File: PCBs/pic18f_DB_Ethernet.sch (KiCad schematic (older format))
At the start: 21 parts

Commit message: TODO: Programming header. TODO: incorporate cabling design for connector modules.
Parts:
- added C? (x2): CAP, symbol pspice:CAP
- added J? (x2): Conn02x05OddEven, symbol Connector_Generic:Conn_02x05_Odd_Even
- added R? (x3): R_US, symbol Device:R_US
- added SW?: SW_DPDT_x2, symbol Switch:SW_DPDT_x2
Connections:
- net 3v3: now also C?.1, C?.1, SW?.5 (B)
- net GNDREF: now also C?.2, C?.2, R?.2, R?.2, R?.2
- net at SW?.1 (A): now also R?.1
- new net: R?.1, SW?.6 (C)
- new net: R?.1, SW?.4 (A)
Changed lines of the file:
@@
 Wire Wire Line
 	2000 3300 2150 3300
+$Comp
+L Device:R_US R?
+U 1 1 5E534EAE
+P 2750 3450
+F 0 "R?" H 2818 3496 50  0000 L CNN
+F 1 "R_US" H 2818 3405 50  0000 L CNN
+F 2 "" V 2790 3440 50  0001 C CNN
+F 3 "~" H 2750 3450 50  0001 C CNN
+	1    2750 3450
+	1    0    0    -1
+$EndComp
+Text GLabel 2450 3600 0    50   Input ~ 0
+GND
+Wire Wire Line
+	2450 3600 2750 3600
+Wire Wire Line
+	2750 3300 2750 3100
+Wire Wire Line
+	2750 3100 2000 3100
+Text GLabel 1300 4050 0    50   Input ~ 0
+3v3
+Wire Wire Line
+	1300 4050 1600 4050
+$Comp
+L Device:R_US R?
+U 1 1 5E5368E4
+P 2150 4300
+F 0 "R?" H 2218 4346 50  0000 L CNN
+F 1 "R_US" H 2218 4255 50  0000 L CNN
+F 2 "" V 2190 4290 50  0001 C CNN
+F 3 "~" H 2150 4300 50  0001 C CNN
+	1    2150 4300
+	1    0    0    -1
+$EndComp
+Text GLabel 1850 4450 0    50   Input ~ 0
+GND
+Wire Wire Line
+	1850 4450 2150 4450
+Wire Wire Line
+	2000 4150 2150 4150
+$Comp
+L Device:R_US R?
+U 1 1 5E5368EE
+P 2750 4300
+F 0 "R?" H 2818 4346 50  0000 L CNN
+F 1 "R_US" H 2818 4255 50  0000 L CNN
+F 2 "" V 2790 4290 50  0001 C CNN
+F 3 "~" H 2750 4300 50  0001 C CNN
+	1    2750 4300
+	1    0    0    -1
+$EndComp
+Text GLabel 2450 4450 0    50   Input ~ 0
+GND
+Wire Wire Line
+	2450 4450 2750 4450
+Wire Wire Line
+	2750 4150 2750 3950
+Wire Wire Line
+	2750 3950 2000 3950
+$Comp
+L Switch:SW_DPDT_x2 SW?
+U 2 1 5E537BD7
+P 1800 4050
+F 0 "SW?" H 1800 4335 50  0000 C CNN
+F 1 "SW_DPDT_x2" H 1800 4244 50  0000 C CNN
+F 2 "" H 1800 4050 50  0001 C CNN
+F 3 "" H 1800 4050 50  0001 C CNN
+	2    1800 4050
+	1    0    0    -1
+$EndComp
+$Comp
+L Connector_Generic:Conn_02x05_Odd_Even J?
+U 1 1 5E53B6D7
+P 7350 2350
+F 0 "J?" V 7354 2630 50  0000 L CNN
+F 1 "Conn02x05OddEven" V 7445 2630 50  0000 L CNN
+F 2 "" H 7350 2350 50  0001 C CNN
+F 3 "~" H 7350 2350 50  0001 C CNN
+	1    7350 2350
+	0    1    1    0
+$EndComp
+$Comp
+L Connector_Generic:Conn_02x05_Odd_Even J?
+U 1 1 5E53C70C
+P 7350 3550
+F 0 "J?" V 7354 3830 50  0000 L CNN
+F 1 "Conn02x05OddEven" V 7445 3830 50  0000 L CNN
+F 2 "" H 7350 3550 50  0001 C CNN
+F 3 "~" H 7350 3550 50  0001 C CNN
+	1    7350 3550
+	0    1    1    0
+$EndComp
+$Comp
+L pspice:CAP C?
+U 1 1 5E53E1CC
+P 1800 4950
+F 0 "C?" H 1978 4996 50  0000 L CNN
+F 1 "CAP" H 1978 4905 50  0000 L CNN
+F 2 "" H 1800 4950 50  0001 C CNN
+F 3 "~" H 1800 4950 50  0001 C CNN
+	1    1800 4950
+	1    0    0    -1
+$EndComp
+$Comp
+L pspice:CAP C?
+U 1 1 5E53E5BB
+P 2350 4950
+F 0 "C?" H 2528 4996 50  0000 L CNN
+F 1 "CAP" H 2528 4905 50  0000 L CNN
+F 2 "" H 2350 4950 50  0001 C CNN
+F 3 "~" H 2350 4950 50  0001 C CNN
+	1    2350 4950
+	1    0    0    -1
+$EndComp
+Text GLabel 1300 4700 0    50   Input ~ 0
+3v3
+Text GLabel 1300 5200 0    50   Input ~ 0
+GND
+Wire Wire Line
+	1300 5200 1800 5200
+Connection ~ 1800 5200
+Wire Wire Line
+	1800 5200 2350 5200
+Wire Wire Line
+	1300 4700 1800 4700
+Connection ~ 1800 4700
+Wire Wire Line
+	1800 4700 2350 4700
 $EndSCHEMATC

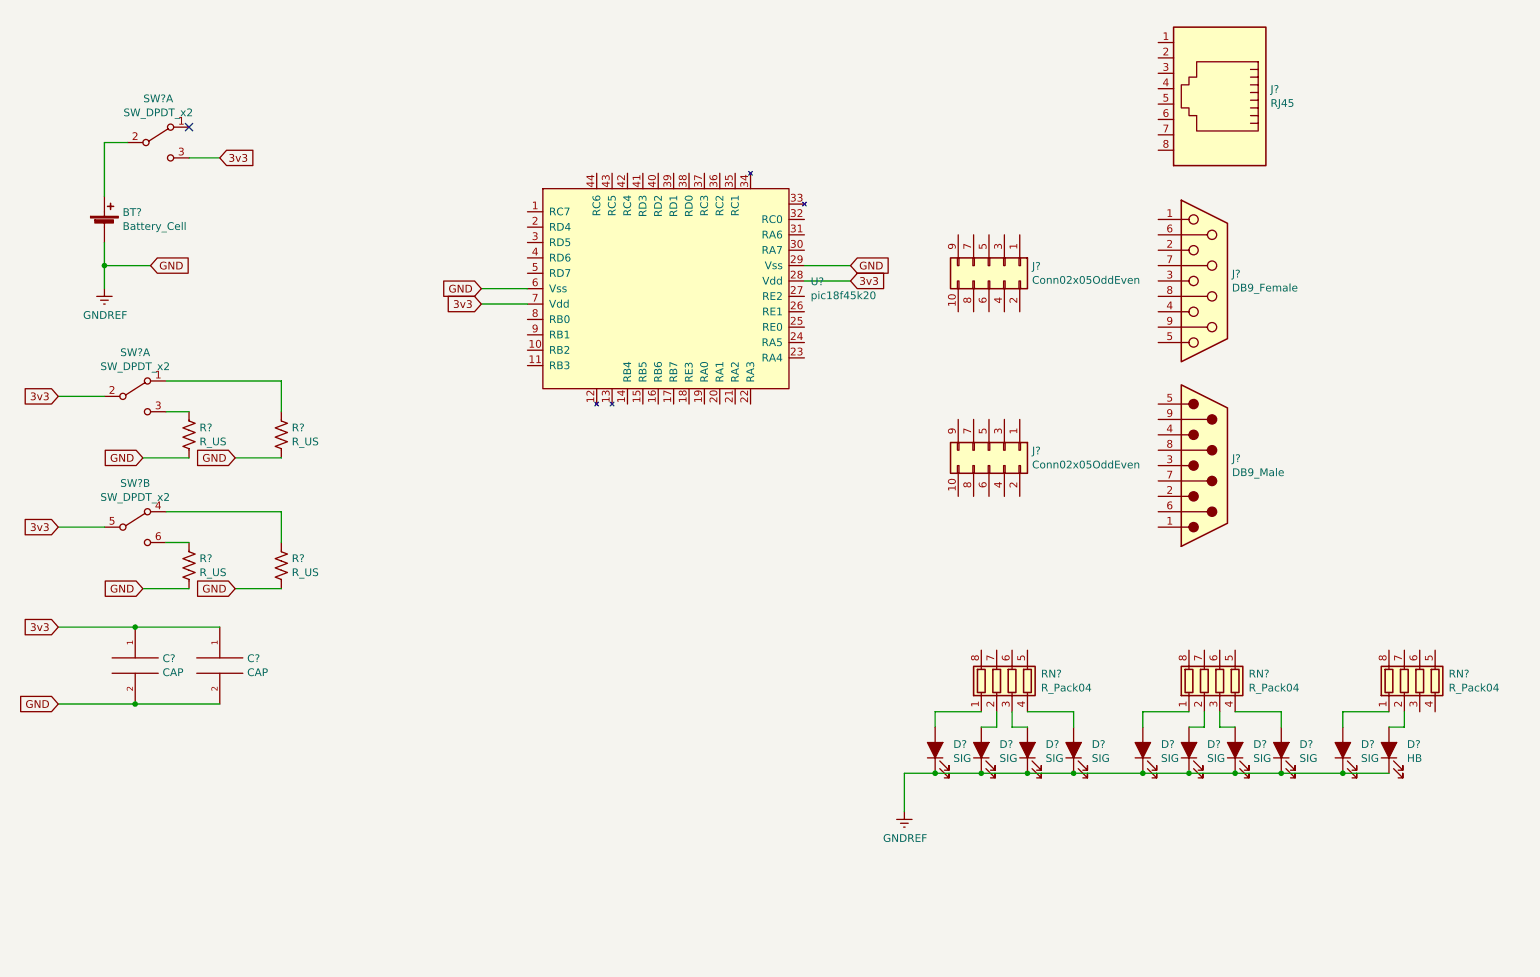
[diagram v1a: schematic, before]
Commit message: some basic connections laid down. TODO: double check I2C pins. Programming pins. And inputs.
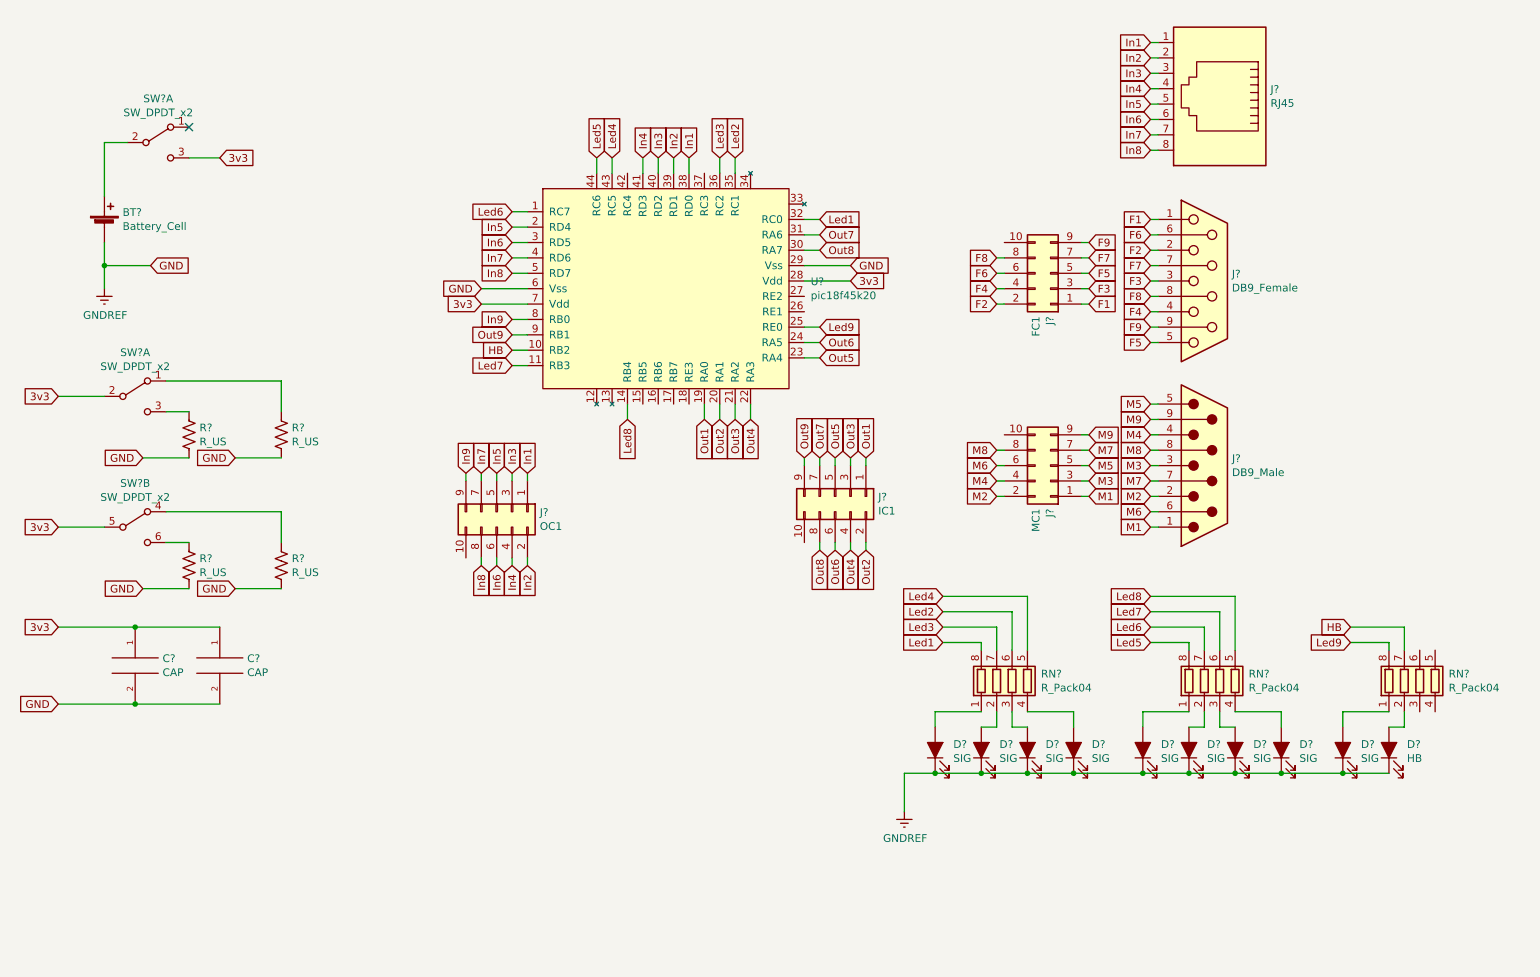
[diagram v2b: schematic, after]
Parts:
- added J?: OC1, symbol Connector_Generic:Conn_02x05_Odd_Even
- added J?: IC1, symbol Connector_Generic:Conn_02x05_Odd_Even
- J?: value Conn02x05OddEven -> FC1
- J?: value Conn02x05OddEven -> MC1
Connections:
- net In1: now reaches J?.1
- net In1: now also U?.38 (RD0), J?.1 (Pin_1)
- net In2: now reaches J?.2
- net In2: now also U?.39 (RD1), J?.2 (Pin_2)
- net In3: now reaches J?.3
- net In3: now also U?.40 (RD2), J?.3 (Pin_3)
- net In4: now reaches J?.4
- net In4: now also U?.41 (RD3), J?.4 (Pin_4)
- net In5: now reaches J?.5
- net In5: now also U?.2 (RD4), J?.5 (Pin_5)
- net In6: now reaches J?.6
- net In6: now also U?.3 (RD5), J?.6 (Pin_6)
- net In7: now reaches J?.7
- net In7: now also U?.4 (RD6), J?.7 (Pin_7)
- net In8: now reaches J?.8
- net In8: now also U?.5 (RD7), J?.8 (Pin_8)
- net F1: now reaches J?.1
- net F1: now also J?.1 (Pin_1)
- net F2: now reaches J?.2
- net F2: now also J?.2 (Pin_2)
- net F3: now reaches J?.3
- net F3: now also J?.3 (Pin_3)
- net F4: now reaches J?.4
- net F4: now also J?.4 (Pin_4)
- net F5: now reaches J?.5
- net F5: now also J?.5 (Pin_5)
- net F6: now reaches J?.6
- net F6: now also J?.6 (Pin_6)
- net F7: now reaches J?.7
- net F7: now also J?.7 (Pin_7)
- net F8: now reaches J?.8
- net F8: now also J?.8 (Pin_8)
- net F9: now reaches J?.9
- net F9: now also J?.9 (Pin_9)
- net M1: now reaches J?.1
- net M1: now also J?.1 (Pin_1)
- net M2: now reaches J?.2
- net M2: now also J?.2 (Pin_2)
- net M3: now reaches J?.3
- net M3: now also J?.3 (Pin_3)
- net M4: now reaches J?.4
- net M4: now also J?.4 (Pin_4)
- net M5: now reaches J?.5
- net M5: now also J?.5 (Pin_5)
- net M6: now reaches J?.6
- net M6: now also J?.6 (Pin_6)
- net M7: now reaches J?.7
- net M7: now also J?.7 (Pin_7)
- net M8: now reaches J?.8
- net M8: now also J?.8 (Pin_8)
- net M9: now reaches J?.9
- net M9: now also J?.9 (Pin_9)
- net Led4: now reaches RN?.5 (R4.2)
- net Led4: now also U?.43 (RC5)
- net Led2: now reaches RN?.6 (R3.2)
- net Led2: now also U?.35 (RC1)
- net Led3: now reaches RN?.7 (R2.2)
- net Led3: now also U?.36 (RC2)
- net Led1: now reaches RN?.8 (R1.2)
- net Led1: now also U?.32 (RC0)
- net Led8: now reaches RN?.5 (R4.2)
- net Led8: now also U?.14 (RB4)
- net Led7: now reaches RN?.6 (R3.2)
- net Led7: now also U?.11 (RB3)
- net Led6: now reaches RN?.7 (R2.2)
- net Led6: now also U?.1 (RC7)
- net Led5: now reaches RN?.8 (R1.2)
- net Led5: now also U?.44 (RC6)
- net HB: now reaches RN?.7 (R2.2)
- net HB: now also U?.10 (RB2)
- net Led9: now reaches RN?.8 (R1.2)
- net Led9: now also U?.25 (RE0)
- net Out1: now reaches U?.19 (RA0)
- net Out1: now also J?.1 (Pin_1)
- net Out2: now reaches U?.20 (RA1)
- net Out2: now also J?.2 (Pin_2)
- net Out3: now reaches U?.21 (RA2)
- net Out3: now also J?.3 (Pin_3)
- net Out4: now reaches U?.22 (RA3)
- net Out4: now also J?.4 (Pin_4)
- net Out5: now reaches U?.23 (RA4)
- net Out5: now also J?.5 (Pin_5)
- net Out6: now reaches U?.24 (RA5)
- net Out6: now also J?.6 (Pin_6)
- net Out8: now reaches U?.30 (RA7)
- net Out8: now also J?.8 (Pin_8)
- net Out7: now reaches U?.31 (RA6)
- net Out7: now also J?.7 (Pin_7)
- net In9: now reaches U?.8 (RB0)
- net In9: now also J?.9 (Pin_9)
- net Out9: now reaches U?.9 (RB1)
- net Out9: now also J?.9 (Pin_9)
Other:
- moved on the sheet: J?

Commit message: Finished basic schematic
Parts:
- added J2: PicKIT 3, symbol Connector:Conn_01x06_Female
- added R5: 10K, symbol Device:R_US
- BT1: renamed from BT?; value Battery_Cell -> CR2032
- RN1, RN2, RN3: renamed from RN?; value R_Pack04 -> 1.1K
- SW2: renamed from SW?; value SW_DPDT_x2 -> PWR_SW
- gave numbers to parts that had none: 25
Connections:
- net 3v3: now also J2.2 (Pin_2), R5.1
- net GNDREF: now also J2.3 (Pin_3)
- net at U1.15 (RB5): now also J2.6 (Pin_6)
- net at U1.16 (RB6): now also J2.5 (Pin_5)
- net at U1.17 (RB7): now also J2.4 (Pin_4)
- net at U1.18 (RE3): now also J2.1 (Pin_1), R5.2
- net SW1: now reaches U1.26 (RE1)
- net SW1: now also R1.1, SW1.3 (C)
- net SW0: now reaches U1.27 (RE2)
- net SW0: now also R3.1, SW1.1 (A)
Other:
- note added: "Top"

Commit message: generated a basic net list
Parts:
- C1, C2: footprint (none) -> Capacitor_SMD:C_0805_2012Metric
- D1, D10, D2, D3, D4, D5, D6, D7, D8, D9: footprint (none) -> LED_SMD:LED_0603_1608Metric
- J1, J3, J4, J5: footprint (none) -> Connector_PinHeader_2.54mm:PinHeader_2x05_P2.54mm_Vertical
- J2: footprint (none) -> Connector_PinHeader_2.54mm:PinHeader_1x06_P2.54mm_Vertical
- J6, J7: footprint (none) -> Connector_Dsub:DSUB-9_Female_Horizontal_P2.77x2.84mm_EdgePinOffset9.90mm_Housed_MountingHolesOffset11.32mm
- J8: footprint (none) -> Connector_RJ:RJ45_Amphenol_RJHSE5380
- R1, R2, R3, R4, R5: footprint (none) -> Resistor_SMD:R_0603_1608Metric
- RN1, RN2, RN3: footprint (none) -> Resistor_SMD:R_Array_Concave_4x0603
- U1: footprint (none) -> Package_QFP:LQFP-44_10x10mm_P0.8mm
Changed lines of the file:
@@
 F 0 "J8" H 8520 1204 50  0000 R CNN
 F 1 "RJ45" H 8520 1295 50  0000 R CNN
-F 2 "" V 8850 1225 50  0001 C CNN
+F 2 "Connector_RJ:RJ45_Amphenol_RJHSE5380" V 8850 1225 50  0001 C CNN
 F 3 "~" V 8850 1225 50  0001 C CNN
 	1    8850 1200
@@
 F 0 "J6" H 8929 2496 50  0000 L CNN
 F 1 "DB9_Female" H 8929 2405 50  0000 L CNN
-F 2 "" H 8750 2450 50  0001 C CNN
+F 2 "Connector_Dsub:DSUB-9_Female_Horizontal_P2.77x2.84mm_EdgePinOffset9.90mm_Housed_MountingHolesOffset11.32mm" H 8750 2450 50  0001 C CNN
 F 3 " ~" H 8750 2450 50  0001 C CNN
 	1    8750 2450
@@
 F 0 "J7" H 8930 3696 50  0000 L CNN
 F 1 "DB9_Male" H 8930 3605 50  0000 L CNN
-F 2 "" H 8750 3650 50  0001 C CNN
+F 2 "Connector_Dsub:DSUB-9_Female_Horizontal_P2.77x2.84mm_EdgePinOffset9.90mm_Housed_MountingHolesOffset11.32mm" H 8750 3650 50  0001 C CNN
 F 3 " ~" H 8750 3650 50  0001 C CNN
 	1    8750 3650
@@
 F 0 "D1" V 7038 5382 50  0000 R CNN
 F 1 "SIG" V 6947 5382 50  0000 R CNN
-F 2 "" H 7000 5500 50  0001 C CNN
+F 2 "LED_SMD:LED_0603_1608Metric" H 7000 5500 50  0001 C CNN
 F 3 "~" H 7000 5500 50  0001 C CNN
 	1    7000 5500
@@
 F 0 "D2" V 7338 5382 50  0000 R CNN
 F 1 "SIG" V 7247 5382 50  0000 R CNN
-F 2 "" H 7300 5500 50  0001 C CNN
+F 2 "LED_SMD:LED_0603_1608Metric" H 7300 5500 50  0001 C CNN
 F 3 "~" H 7300 5500 50  0001 C CNN
 	1    7300 5500
@@
 F 0 "D3" V 7638 5382 50  0000 R CNN
 F 1 "SIG" V 7547 5382 50  0000 R CNN
-F 2 "" H 7600 5500 50  0001 C CNN
+F 2 "LED_SMD:LED_0603_1608Metric" H 7600 5500 50  0001 C CNN
 F 3 "~" H 7600 5500 50  0001 C CNN
 	1    7600 5500
@@
 F 0 "D4" V 7938 5382 50  0000 R CNN
 F 1 "SIG" V 7847 5382 50  0000 R CNN
-F 2 "" H 7900 5500 50  0001 C CNN
+F 2 "LED_SMD:LED_0603_1608Metric" H 7900 5500 50  0001 C CNN
 F 3 "~" H 7900 5500 50  0001 C CNN
 	1    7900 5500
@@
 F 0 "RN1" H 7688 5096 50  0000 L CNN
 F 1 "1.1K" H 7688 5005 50  0000 L CNN
-F 2 "" V 7775 5050 50  0001 C CNN
+F 2 "Resistor_SMD:R_Array_Concave_4x0603" V 7775 5050 50  0001 C CNN
 F 3 "~" H 7500 5050 50  0001 C CNN
 	1    7500 5050
@@
 F 0 "D5" V 8388 5382 50  0000 R CNN
 F 1 "SIG" V 8297 5382 50  0000 R CNN
-F 2 "" H 8350 5500 50  0001 C CNN
+F 2 "LED_SMD:LED_0603_1608Metric" H 8350 5500 50  0001 C CNN
 F 3 "~" H 8350 5500 50  0001 C CNN
 	1    8350 5500
@@
 F 0 "D6" V 8688 5382 50  0000 R CNN
 F 1 "SIG" V 8597 5382 50  0000 R CNN
-F 2 "" H 8650 5500 50  0001 C CNN
+F 2 "LED_SMD:LED_0603_1608Metric" H 8650 5500 50  0001 C CNN
 F 3 "~" H 8650 5500 50  0001 C CNN
 	1    8650 5500
@@
 F 0 "D7" V 8988 5382 50  0000 R CNN
 F 1 "SIG" V 8897 5382 50  0000 R CNN
-F 2 "" H 8950 5500 50  0001 C CNN
+F 2 "LED_SMD:LED_0603_1608Metric" H 8950 5500 50  0001 C CNN
 F 3 "~" H 8950 5500 50  0001 C CNN
 	1    8950 5500
@@
 F 0 "D8" V 9288 5382 50  0000 R CNN
 F 1 "SIG" V 9197 5382 50  0000 R CNN
-F 2 "" H 9250 5500 50  0001 C CNN
+F 2 "LED_SMD:LED_0603_1608Metric" H 9250 5500 50  0001 C CNN
 F 3 "~" H 9250 5500 50  0001 C CNN
 	1    9250 5500
@@
 F 0 "RN2" H 9038 5096 50  0000 L CNN
 F 1 "1.1K" H 9038 5005 50  0000 L CNN
-F 2 "" V 9125 5050 50  0001 C CNN
+F 2 "Resistor_SMD:R_Array_Concave_4x0603" V 9125 5050 50  0001 C CNN
 F 3 "~" H 8850 5050 50  0001 C CNN
 	1    8850 5050
@@
 F 0 "D9" V 9688 5382 50  0000 R CNN
 F 1 "SIG" V 9597 5382 50  0000 R CNN
-F 2 "" H 9650 5500 50  0001 C CNN
+F 2 "LED_SMD:LED_0603_1608Metric" H 9650 5500 50  0001 C CNN
 F 3 "~" H 9650 5500 50  0001 C CNN
 	1    9650 5500
@@
 F 0 "D10" V 9988 5383 50  0000 R CNN
 F 1 "HB" V 9897 5383 50  0000 R CNN
-F 2 "" H 9950 5500 50  0001 C CNN
+F 2 "LED_SMD:LED_0603_1608Metric" H 9950 5500 50  0001 C CNN
 F 3 "~" H 9950 5500 50  0001 C CNN
 	1    9950 5500
@@
 F 0 "RN3" H 10338 5096 50  0000 L CNN
 F 1 "1.1K" H 10338 5005 50  0000 L CNN
-F 2 "" V 10425 5050 50  0001 C CNN
+F 2 "Resistor_SMD:R_Array_Concave_4x0603" V 10425 5050 50  0001 C CNN
 F 3 "~" H 10150 5050 50  0001 C CNN
 	1    10150 5050
@@
 F 0 "U1" H 5300 2550 50  0000 L CNN
 F 1 "pic18f45k20" H 5300 2450 50  0000 L CNN
-F 2 "" H 5300 2500 50  0001 C CNN
+F 2 "Package_QFP:LQFP-44_10x10mm_P0.8mm" H 5300 2500 50  0001 C CNN
 F 3 "" H 5300 2500 50  0001 C CNN
 	1    5300 2500
@@
 F 0 "R1" H 2218 3496 50  0000 L CNN
 F 1 "R_US" H 2218 3405 50  0000 L CNN
-F 2 "" V 2190 3440 50  0001 C CNN
+F 2 "Resistor_SMD:R_0603_1608Metric" V 2190 3440 50  0001 C CNN
 F 3 "~" H 2150 3450 50  0001 C CNN
 	1    2150 3450
@@
 F 0 "R3" H 2818 3496 50  0000 L CNN
 F 1 "R_US" H 2818 3405 50  0000 L CNN
-F 2 "" V 2790 3440 50  0001 C CNN
+F 2 "Resistor_SMD:R_0603_1608Metric" V 2790 3440 50  0001 C CNN
 F 3 "~" H 2750 3450 50  0001 C CNN
 	1    2750 3450
@@
 F 0 "R2" H 2218 4346 50  0000 L CNN
 F 1 "R_US" H 2218 4255 50  0000 L CNN
-F 2 "" V 2190 4290 50  0001 C CNN
+F 2 "Resistor_SMD:R_0603_1608Metric" V 2190 4290 50  0001 C CNN
 F 3 "~" H 2150 4300 50  0001 C CNN
 	1    2150 4300
@@
 F 0 "R4" H 2818 4346 50  0000 L CNN
 F 1 "R_US" H 2818 4255 50  0000 L CNN
-F 2 "" V 2790 4290 50  0001 C CNN
+F 2 "Resistor_SMD:R_0603_1608Metric" V 2790 4290 50  0001 C CNN
 F 3 "~" H 2750 4300 50  0001 C CNN
 	1    2750 4300
@@
 F 0 "J4" V 7754 2680 50  0000 L CNN
 F 1 "FC1" V 7845 2680 50  0000 L CNN
-F 2 "" H 7750 2400 50  0001 C CNN
+F 2 "Connector_PinHeader_2.54mm:PinHeader_2x05_P2.54mm_Vertical" H 7750 2400 50  0001 C CNN
 F 3 "~" H 7750 2400 50  0001 C CNN
 	1    7750 2400
@@
 F 0 "J5" V 7754 3930 50  0000 L CNN
 F 1 "MC1" V 7845 3930 50  0000 L CNN
-F 2 "" H 7750 3650 50  0001 C CNN
+F 2 "Connector_PinHeader_2.54mm:PinHeader_2x05_P2.54mm_Vertical" H 7750 3650 50  0001 C CNN
 F 3 "~" H 7750 3650 50  0001 C CNN
 	1    7750 3650
@@
 F 0 "C1" H 1978 4996 50  0000 L CNN
 F 1 "CAP" H 1978 4905 50  0000 L CNN
-F 2 "" H 1800 4950 50  0001 C CNN
+F 2 "Capacitor_SMD:C_0805_2012Metric" H 1800 4950 50  0001 C CNN
 F 3 "~" H 1800 4950 50  0001 C CNN
 	1    1800 4950
@@
 F 0 "C2" H 2528 4996 50  0000 L CNN
 F 1 "CAP" H 2528 4905 50  0000 L CNN
-F 2 "" H 2350 4950 50  0001 C CNN
+F 2 "Capacitor_SMD:C_0805_2012Metric" H 2350 4950 50  0001 C CNN
 F 3 "~" H 2350 4950 50  0001 C CNN
 	1    2350 4950
@@
 F 0 "J1" V 4154 4230 50  0000 L CNN
 F 1 "OC1" V 4245 4230 50  0000 L CNN
-F 2 "" H 4150 3950 50  0001 C CNN
+F 2 "Connector_PinHeader_2.54mm:PinHeader_2x05_P2.54mm_Vertical" H 4150 3950 50  0001 C CNN
 F 3 "~" H 4150 3950 50  0001 C CNN
 	1    4150 3950
@@
 F 0 "J3" V 6354 4130 50  0000 L CNN
 F 1 "IC1" V 6445 4130 50  0000 L CNN
-F 2 "" H 6350 3850 50  0001 C CNN
+F 2 "Connector_PinHeader_2.54mm:PinHeader_2x05_P2.54mm_Vertical" H 6350 3850 50  0001 C CNN
 F 3 "~" H 6350 3850 50  0001 C CNN
 	1    6350 3850
@@
 F 0 "J2" V 5300 4100 50  0000 L CNN
 F 1 "PicKIT 3" V 5400 4100 50  0000 L CNN
-F 2 "" H 5250 4100 50  0001 C CNN
+F 2 "Connector_PinHeader_2.54mm:PinHeader_1x06_P2.54mm_Vertical" H 5250 4100 50  0001 C CNN
 F 3 "~" H 5250 4100 50  0001 C CNN
 	1    5250 4100
@@
 F 0 "R5" V 5395 3900 50  0000 C CNN
 F 1 "10K" V 5486 3900 50  0000 C CNN
-F 2 "" V 5640 3890 50  0001 C CNN
+F 2 "Resistor_SMD:R_0603_1608Metric" V 5640 3890 50  0001 C CNN
 F 3 "~" H 5600 3900 50  0001 C CNN
 	1    5600 3900
